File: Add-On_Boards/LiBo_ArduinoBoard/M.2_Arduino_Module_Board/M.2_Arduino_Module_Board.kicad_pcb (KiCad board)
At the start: 2 copper layers, 53.6 x 68.8 mm, 15 parts, among them J2 2199230-3, J3 USB_C_Receptacle_USB2.0, U1 USBLC6-2SC6, U2 TLV62568DBV

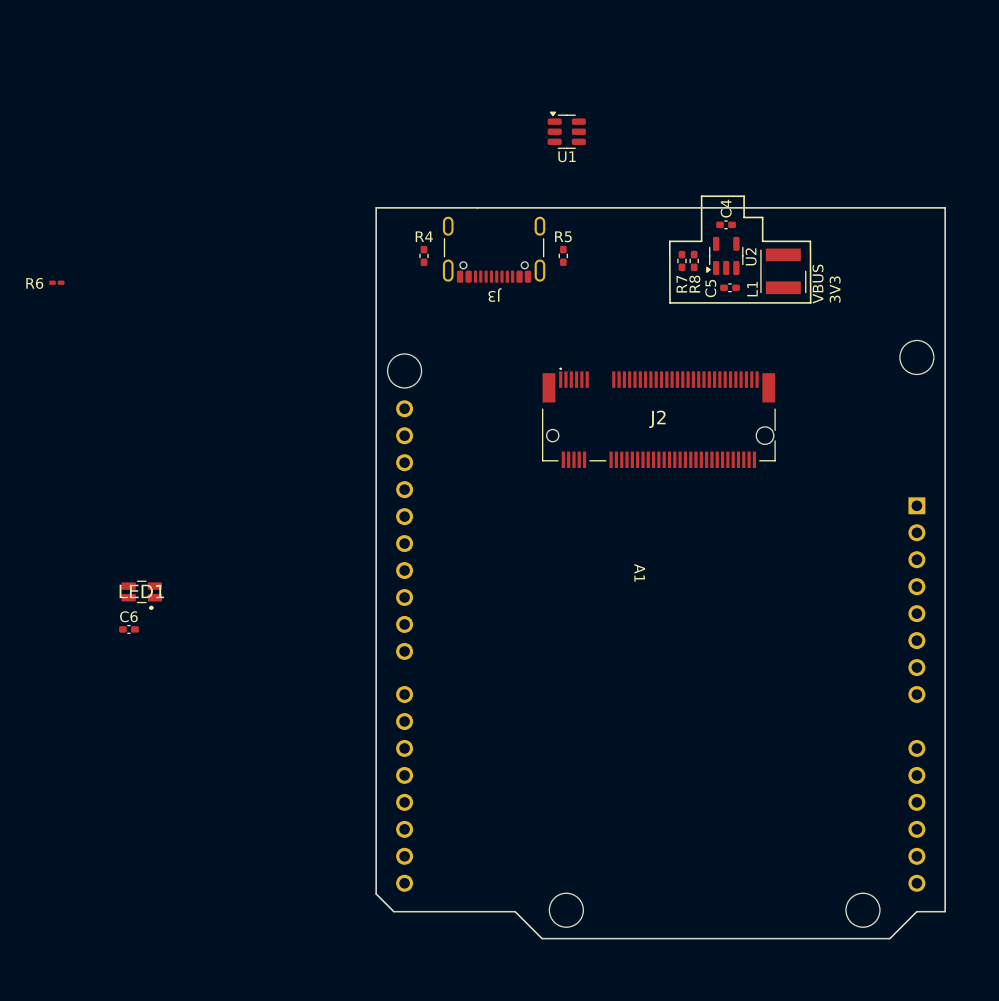
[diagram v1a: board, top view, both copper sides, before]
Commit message: Changes to ArduinoBoard
Needed:
1. Diodes.
2. Status LEDS
3. Footprint checking
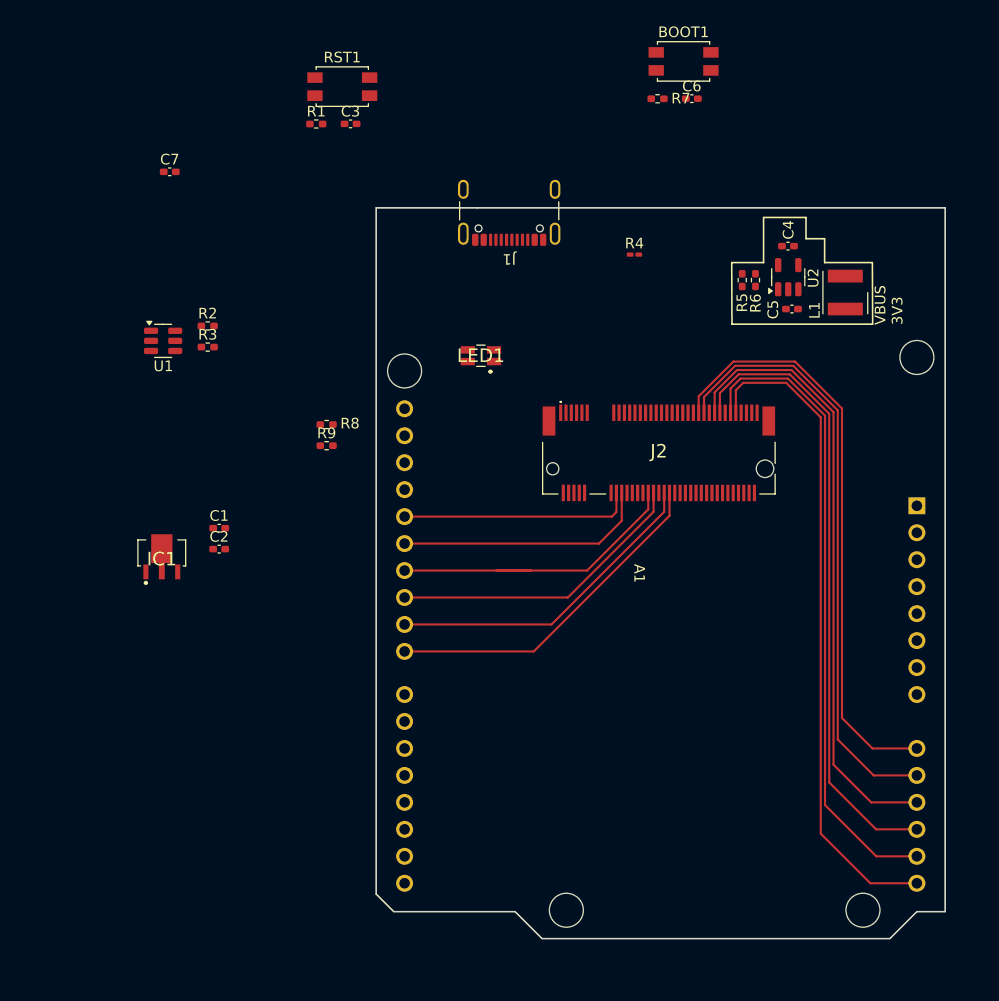
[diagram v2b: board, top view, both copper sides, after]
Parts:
- removed J3: USB_C_Receptacle_USB2.0, Connector_USB:USB_C_Receptacle_GCT_USB4105-xx-A_16P_TopMnt_Horizontal
- added BOOT1: SW_BOOT, Button_Switch_SMD:SW_SPST_EVQP2, F.Cu at (187.3, 22.5)
- added C1: 1u, Capacitor_SMD:C_0402_1005Metric_Pad0.74x0.62mm_HandSolder, F.Cu at (143.6, 66.5)
- added C2: 1u, Capacitor_SMD:C_0402_1005Metric_Pad0.74x0.62mm_HandSolder, F.Cu at (143.6, 68.5)
- added C3: 100n, Capacitor_SMD:C_0402_1005Metric_Pad0.74x0.62mm_HandSolder, F.Cu at (155.9, 28.4)
- added C7: 100n, Capacitor_SMD:C_0402_1005Metric_Pad0.74x0.62mm_HandSolder, F.Cu at (138.9, 32.9)
- added IC1: MCP1702T-5002E_MB, GitHub_Library:MCP1703T5002EMB, F.Cu at (138.2, 70.0)
- added J1: USB_C_Receptacle_USB2.0, Connector_USB:USB_C_Receptacle_GCT_USB4105-xx-A_16P_TopMnt_Horizontal, F.Cu at (170.9, 35.6)
- added R1: 10k, Resistor_SMD:R_0402_1005Metric_Pad0.72x0.64mm_HandSolder, F.Cu at (152.7, 28.4)
- added R2: 5k1, Resistor_SMD:R_0402_1005Metric_Pad0.72x0.64mm_HandSolder, F.Cu at (142.5, 47.4)
- added R3: 5k1, Resistor_SMD:R_0402_1005Metric_Pad0.72x0.64mm_HandSolder, F.Cu at (142.5, 49.4)
- added R9: 5k1, Resistor_SMD:R_0402_1005Metric_Pad0.72x0.64mm_HandSolder, F.Cu at (153.7, 58.7)
- added RST1: SW_RST, Button_Switch_SMD:SW_SPST_EVQP2, F.Cu at (155.2, 24.9)
- A1: footprint PCB_Lib_DaanHeetkamp_KiCad:Arduino_Uno_Footprint -> GitHub_Library:Arduino_Uno_Footprint
- J2: footprint SamacSys_Parts:21992303 -> GitHub_Library:21992303
- LED1: footprint PCB_Lib_DaanHeetkamp_KiCad:WS2812C2020 -> GitHub_Library:WS2812C2020
- R4: value 5k1 -> 10k; footprint Resistor_SMD:R_0402_1005Metric_Pad0.72x0.64mm_HandSolder -> Resistor_SMD:R_0201_0603Metric_Pad0.64x0.40mm_HandSolder
- R5: value 5k1 -> 450k
- R6: value 10k -> 100k; footprint Resistor_SMD:R_0201_0603Metric_Pad0.64x0.40mm_HandSolder -> Resistor_SMD:R_0402_1005Metric_Pad0.72x0.64mm_HandSolder
- R7: value 450k -> 10k
- R8: value 100k -> 5k1
- moved C6 72.9 mm to (188.1, 26.0)
- moved R6 65.8 mm to (194.1, 43.1), turned to -90 degrees
- moved U1 42.8 mm to (138.3, 48.9)
- moved LED1 38.9 mm to (168.2, 50.2)
- moved R8 37.9 mm to (153.7, 56.7), turned to 0 degrees
- moved R4 19.8 mm to (182.7, 40.7), turned to 0 degrees
- moved R5 17.0 mm to (192.8, 43.1), turned to 90 degrees
- moved R7 15.5 mm to (184.8, 26.0), turned to 180 degrees
- moved L1 6.17 mm to (202.5, 44.3)
- moved U2 6.17 mm to (197.2, 42.9)
- moved C4 6.17 mm to (197.1, 39.9)
- moved C5 6.17 mm to (197.5, 45.9)
- moved J2 3.12 mm to (185.0, 60.9)
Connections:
- A1 pad 10: unconnected-(A1-A1-Pad10) -> /GPIO5
- A1 pad 11: unconnected-(A1-A2-Pad11) -> /GPIO4
- A1 pad 12: unconnected-(A1-A3-Pad12) -> /GPIO3
- A1 pad 13: unconnected-(A1-SDA/A4-Pad13) -> /GPIO2
- A1 pad 14: unconnected-(A1-SCL/A5-Pad14) -> /GPIO1
- A1 pad 15: unconnected-(A1-D0/RX-Pad15) -> /U0RXD
- A1 pad 16: unconnected-(A1-D1/TX-Pad16) -> /U0TXD
- A1 pad 17: unconnected-(A1-D2-Pad17) -> /GPIO7
- A1 pad 18: unconnected-(A1-D3-Pad18) -> /GPIO8
- A1 pad 19: unconnected-(A1-D4-Pad19) -> /GPIO9
- A1 pad 2: unconnected-(A1-IOREF-Pad2) -> +3V3
- A1 pad 20: unconnected-(A1-D5-Pad20) -> /GPIO10
- A1 pad 21: unconnected-(A1-D6-Pad21) -> /GPIO11
- A1 pad 22: unconnected-(A1-D7-Pad22) -> /GPIO12
- A1 pad 23: unconnected-(A1-D8-Pad23) -> /GPIO36
- A1 pad 24: unconnected-(A1-D9-Pad24) -> /GPIO35
- A1 pad 25: unconnected-(A1-D10-Pad25) -> /GPIO34
- A1 pad 26: unconnected-(A1-D11-Pad26) -> /GPIO33
- A1 pad 27: unconnected-(A1-D12-Pad27) -> /GPIO18
- A1 pad 28: unconnected-(A1-D13-Pad28) -> /GPIO17
- A1 pad 29: unconnected-(A1-GND-Pad29) -> Earth
- A1 pad 3: unconnected-(A1-~{RESET}-Pad3) -> /CHIP_PU
- A1 pad 30: unconnected-(A1-AREF-Pad30) -> +3V3
- A1 pad 31: unconnected-(A1-SDA/A4-Pad31) -> /GPIO2
- A1 pad 32: unconnected-(A1-SCL/A5-Pad32) -> /GPIO1
- A1 pad 4: unconnected-(A1-3V3-Pad4) -> +3V3
- A1 pad 5: unconnected-(A1-+5V-Pad5) -> +5V
- A1 pad 6: unconnected-(A1-GND-Pad6) -> Earth
- A1 pad 7: unconnected-(A1-GND-Pad7) -> Earth
- A1 pad 8: unconnected-(A1-VIN-Pad8) -> VBUS
- A1 pad 9: unconnected-(A1-A0-Pad9) -> /GPIO6
- C6 pad 1: +3V3 -> /CHIP_BOOT
- J2 pad 22: /GPIO18 -> /GPIO17
- J2 pad 24: /GPIO17 -> /GPIO18
- R4 pad 1: /USB_CC2 -> VBUS
- R4 pad 2: Earth -> Net-(U2-EN)
- R5 pad 1: /USB_CC1 -> +3V3
- R5 pad 2: Earth -> Net-(U2-FB)
- R6 pad 1: VBUS -> Net-(U2-FB)
- R6 pad 2: Net-(U2-EN) -> Earth
- R7 pad 2: Net-(U2-FB) -> /CHIP_BOOT
- R8 pad 1: Net-(U2-FB) -> +3V3
- R8 pad 2: Earth -> /GPIO2
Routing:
- net /GPIO1: track 0.00 -> 62.0 mm
- net /GPIO2: track 0.00 -> 60.4 mm
- net /GPIO3: track 0.00 -> 59.2 mm
- net /GPIO4: track 0.00 -> 58.2 mm
- net /GPIO5: track 0.00 -> 56.9 mm
- net /GPIO6: track 0.00 -> 55.6 mm
- net /GPIO36: track 0.00 -> 32.4 mm
- net /GPIO35: track 0.00 -> 30.6 mm
- net /GPIO33: track 0.00 -> 30.2 mm
- net /GPIO34: track 0.00 -> 28.6 mm
- net /GPIO18: track 0.00 -> 24.0 mm
- net /GPIO17: track 0.00 -> 21.9 mm

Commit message: first release
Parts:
- removed C4: 4u7, Capacitor_SMD:C_0402_1005Metric_Pad0.74x0.62mm_HandSolder
- removed C5: 10u, Capacitor_SMD:C_0402_1005Metric_Pad0.74x0.62mm_HandSolder
- removed L1: 2u2, Inductor_SMD_Wurth:L_Wurth_WE-LQSH-4020
- removed R4: 10k, Resistor_SMD:R_0201_0603Metric_Pad0.64x0.40mm_HandSolder
- removed R5: 450k, Resistor_SMD:R_0402_1005Metric_Pad0.72x0.64mm_HandSolder
- removed R6: 100k, Resistor_SMD:R_0402_1005Metric_Pad0.72x0.64mm_HandSolder
- removed U2: TLV62568DBV, Package_TO_SOT_SMD:SOT-23-5
- added ?: , , F.Cu at (185.0, 99.7)
- added G***: LOGO, LOGO, F.Cu at (165.2, 58.6)
- added G***: LOGO, LOGO, B.Cu at (198.4, 73.6)
- added G***: LOGO, LOGO, B.Cu at (174.5, 77.0)
- A1, R8, R9: moved to B.Cu
- moved C7 67.4 mm to (202.6, 55.1), turned to 90 degrees
- moved R3 58.5 mm to (200.7, 43.1), turned to -90 degrees
- moved R8 53.3 mm to (206.9, 59.6)
- moved R9 53.3 mm to (206.9, 57.0)
- moved U1 49.9 mm to (188.1, 48.6), turned to 180 degrees
- moved R2 46.2 mm to (188.4, 43.1), turned to -90 degrees
- moved IC1 42.7 mm to (172.4, 44.5), turned to -90 degrees
- moved C1 40.0 mm to (177.2, 45.0), turned to -90 degrees
- moved C2 34.1 mm to (171.2, 48.6), turned to 180 degrees
- moved LED1 32.1 mm to (199.8, 55.9), turned to 90 degrees
- moved BOOT1 31.0 mm to (208.9, 44.8), turned to -90 degrees
- moved R7 26.8 mm to (205.1, 43.5), turned to -90 degrees
- moved C6 26.5 mm to (205.1, 46.3), turned to -90 degrees
- moved J1 24.4 mm to (194.6, 41.2)
- moved R1 22.2 mm to (165.6, 46.5), turned to 90 degrees
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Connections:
- A1 pad 17: /GPIO7 -> /GPIO17
- A1 pad 18: /GPIO8 -> /GPIO18
- A1 pad 19: /GPIO9 -> /GPIO33
- A1 pad 20: /GPIO10 -> /GPIO34
- A1 pad 21: /GPIO11 -> /GPIO35
- A1 pad 22: /GPIO12 -> /GPIO36
- A1 pad 23: /GPIO36 -> /GPIO12
- A1 pad 24: /GPIO35 -> /GPIO11
- A1 pad 25: /GPIO34 -> /GPIO10
- A1 pad 26: /GPIO33 -> /GPIO9
- A1 pad 27: /GPIO18 -> /GPIO8
- A1 pad 28: /GPIO17 -> /GPIO7
- LED1 pad 3: /GPIO46 -> /GPIO45
- U1 pad 1: /USB_D+ -> /USB_D-
- U1 pad 4: /USB_D- -> /USB_D+
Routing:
- net +3V3: track 0.00 -> 135.1 mm, vias 0 -> 4
- net VBUS: track 0.00 -> 78.2 mm, vias 0 -> 4
- net /CHIP_PU: track 0.00 -> 71.6 mm, vias 0 -> 2
- net /U0RXD: track 0.00 -> 47.7 mm, vias 0 -> 1
- net /U0TXD: track 0.00 -> 45.2 mm, vias 0 -> 1
- net /GPIO12: track 0.00 -> 43.1 mm
- net /GPIO11: track 0.00 -> 40.2 mm
- net +5V: track 0.00 -> 36.9 mm
- net /GPIO10: track 0.00 -> 36.6 mm
- net /GPIO9: track 0.00 -> 33.7 mm
- net /GPIO8: track 0.00 -> 30.4 mm
- net /GPIO2: track 60.4 -> 89.0 mm, vias 0 -> 1
- net /CHIP_BOOT: track 0.00 -> 28.4 mm, vias 0 -> 2
- net /GPIO7: track 0.00 -> 27.4 mm
- net /GPIO17: track 21.9 -> 48.8 mm
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- added copper zone on B.Cu, net Earth
- added copper zone on F.Cu, net Earth
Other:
- outline, holes or cut-outs redrawn
- board text added: "+3V3"
- board text added: "+5V"
- board text added: "Arduino Module D.Heetkamp 29-8-25 V1"
- board text added: "GND"
- board text added: "GPIO PORTS"
- board text added: "IO0"
- board text added: "IO1"
- board text added: "IO10"
- board text added: "IO11"
- board text added: "IO12"
- board text added: "IO17"
- board text added: "IO18"
- board text added: "IO2"
- board text added: "IO3"
- board text added: "IO33"
- board text added: "IO34"
- board text added: "IO35"
- board text added: "IO36"
- board text added: "IO4"
- board text added: "IO45"
- board text added: "IO5"
- board text added: "IO6"
- board text added: "IO7"
- board text added: "IO8"
- board text added: "IO9"
- board text added: "POWER"
- board text added: "RESET"
- board text added: "RGB"
- board text added: "RST"
- board text added: "RX"
- board text added: "TX"
- board text added: "USB"
- board text added: "VIN"
- board text removed: "VBUS 3V3"

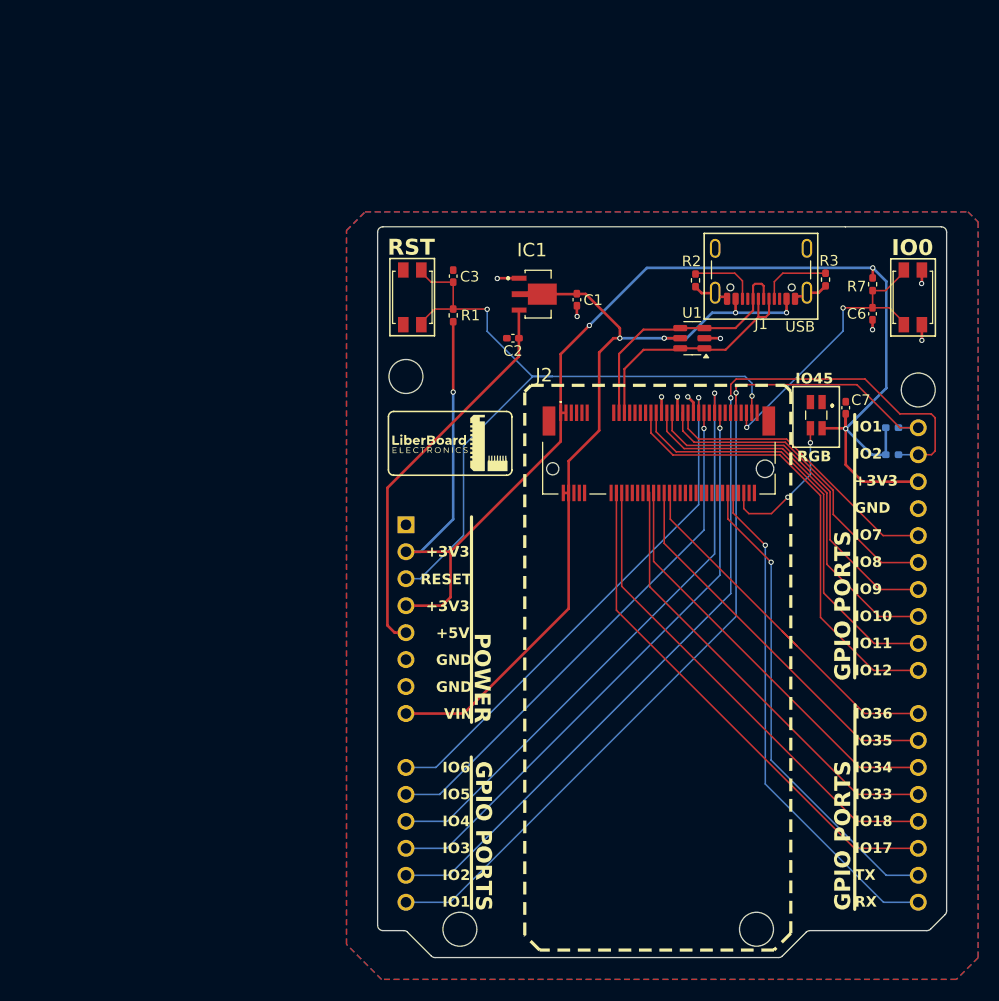
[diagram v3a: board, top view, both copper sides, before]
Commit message: Add new STEP and WRL files for M.2 Arduino and ESP32S3 Boards
- Added M.2 Arduino Module Board STEP file (12633 KB)
- Added ESP32S3 M.2 Board STEP file (16645 KB)
- Added WRL file for unnamed ESP32S3 M.2 Board (2692 KB)
- Created lock file for ESP32S3 M.2 Board project
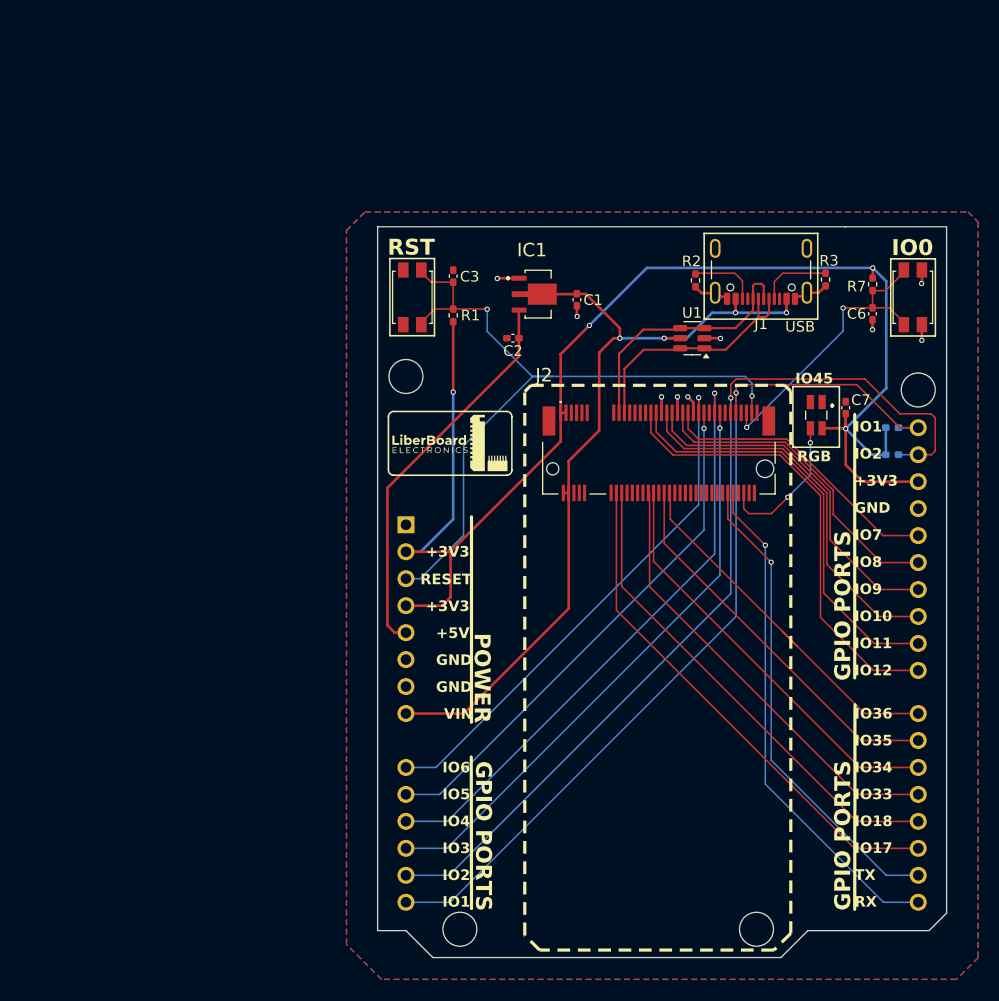
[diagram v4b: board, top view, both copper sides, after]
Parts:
- A1: footprint GitHub_Library:Arduino_Uno_Footprint -> PCB_Lib_DaanHeetkamp_KiCad:Arduino_Uno_Footprint
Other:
- outline, holes or cut-outs redrawn
